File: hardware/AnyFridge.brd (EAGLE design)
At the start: 75.9 x 69.8 mm, 11 parts

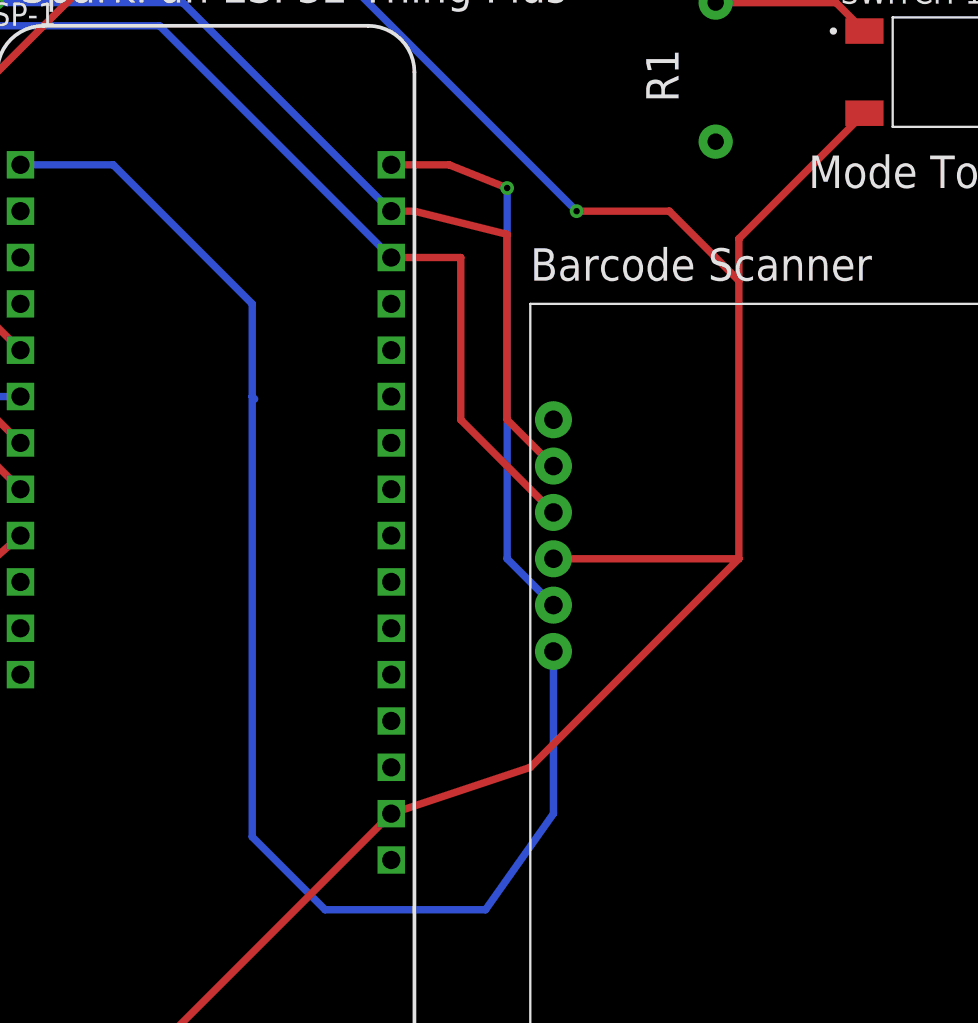
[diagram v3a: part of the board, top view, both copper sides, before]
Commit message: Align all traces to 45deg angles
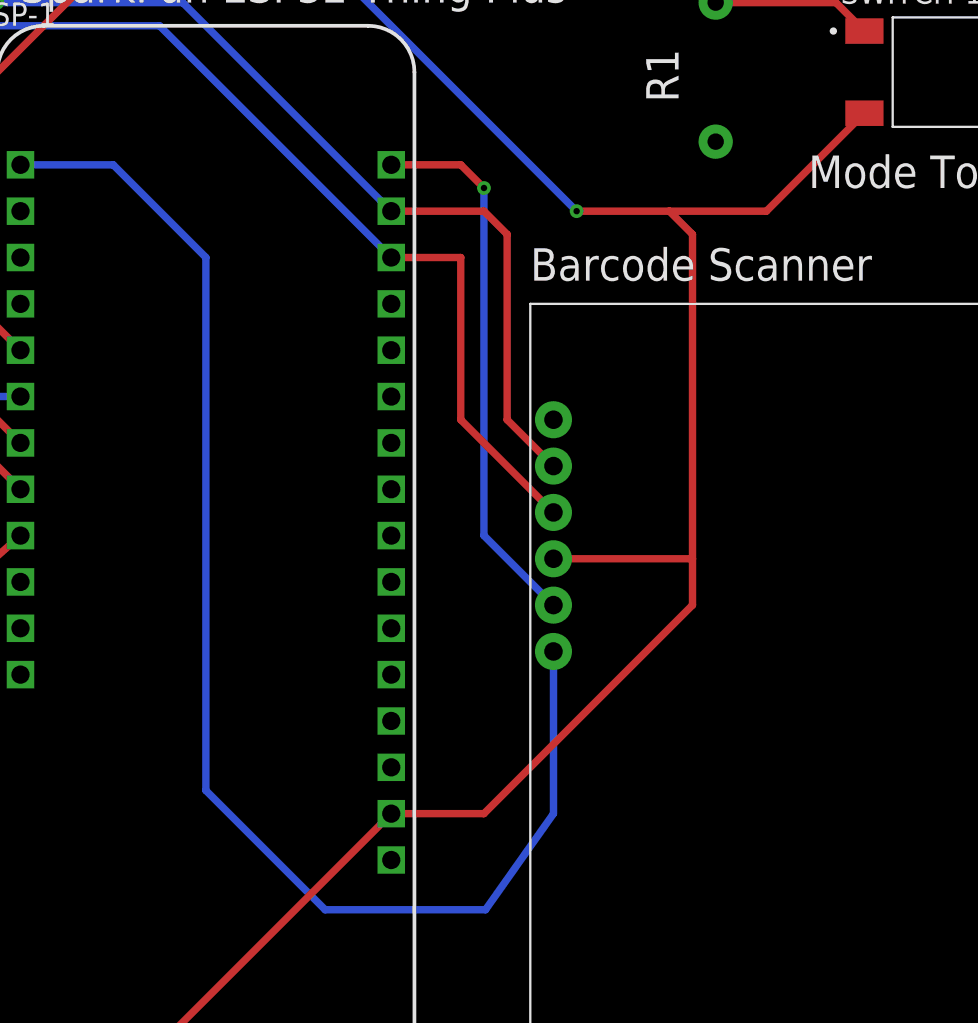
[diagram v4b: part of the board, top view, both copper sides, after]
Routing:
- net 3.3V: track 155.2 -> 152.1 mm
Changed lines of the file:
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@@
 <contactref element="SENS-1" pad="2"/>
 <contactref element="SWITCH-1" pad="2"/>
-<wire x1="66.57" y1="57.44" x2="59.69" y2="50.56" width="0.4064" layer="1"/>
-<wire x1="59.69" y1="50.56" x2="59.69" y2="48.26" width="0.4064" layer="1"/>
-<wire x1="59.69" y1="48.26" x2="59.69" y2="33.02" width="0.4064" layer="1"/>
-<wire x1="59.69" y1="33.02" x2="49.53" y2="33.02" width="0.4064" layer="1"/>
+<wire x1="57.15" y1="50.8" x2="57.15" y2="33.02" width="0.4064" layer="1"/>
+<wire x1="57.15" y1="33.02" x2="57.15" y2="30.48" width="0.4064" layer="1"/>
+<wire x1="57.15" y1="33.02" x2="49.53" y2="33.02" width="0.4064" layer="1"/>
 <contactref element="TP_3.3V" pad="TP"/>
 <wire x1="13.97" y1="66.04" x2="36.83" y2="66.04" width="0.4064" layer="16"/>
@@
 <via x="50.8" y="52.07" extent="1-16" drill="0.35"/>
 <wire x1="50.8" y1="52.07" x2="55.88" y2="52.07" width="0.4064" layer="1"/>
-<wire x1="55.88" y1="52.07" x2="59.69" y2="48.26" width="0.4064" layer="1"/>
+<wire x1="55.88" y1="52.07" x2="57.15" y2="50.8" width="0.4064" layer="1"/>
 <wire x1="40.64" y1="19.05" x2="24.13" y2="2.54" width="0.4064" layer="1"/>
 <wire x1="24.13" y1="2.54" x2="8.89" y2="2.54" width="0.4064" layer="1"/>
 <wire x1="8.89" y1="2.54" x2="8.255" y2="3.175" width="0.4064" layer="1"/>
 <wire x1="8.255" y1="3.175" x2="8.255" y2="4.18" width="0.4064" layer="1"/>
-<wire x1="40.64" y1="19.05" x2="48.26" y2="21.59" width="0.4064" layer="1"/>
-<wire x1="48.26" y1="21.59" x2="59.69" y2="33.02" width="0.4064" layer="1"/>
+<wire x1="57.15" y1="30.48" x2="45.72" y2="19.05" width="0.4064" layer="1"/>
+<wire x1="45.72" y1="19.05" x2="40.64" y2="19.05" width="0.4064" layer="1"/>
+<wire x1="66.57" y1="57.44" x2="61.2" y2="52.07" width="0.4064" layer="1"/>
+<wire x1="61.2" y1="52.07" x2="55.88" y2="52.07" width="0.4064" layer="1"/>
 </signal>
 <signal name="TRIG">
 <contactref element="SCAN-1" pad="TRIG"/>
 <contactref element="ESP-1" pad="21"/>
-<wire x1="46.99" y1="53.34" x2="43.815" y2="54.61" width="0.4064" layer="1"/>
-<wire x1="40.64" y1="54.61" x2="43.815" y2="54.61" width="0.4064" layer="1"/>
-<via x="46.99" y="53.34" extent="1-16" drill="0.35"/>
-<wire x1="46.99" y1="33.02" x2="49.53" y2="30.48" width="0.4064" layer="16"/>
-<wire x1="46.99" y1="33.02" x2="46.99" y2="53.34" width="0.4064" layer="16"/>
+<via x="45.72" y="53.34" extent="1-16" drill="0.35"/>
+<wire x1="45.72" y1="34.29" x2="49.53" y2="30.48" width="0.4064" layer="16"/>
+<wire x1="45.72" y1="53.34" x2="45.72" y2="34.29" width="0.4064" layer="16"/>
+<wire x1="45.72" y1="53.34" x2="44.45" y2="54.61" width="0.4064" layer="1"/>
+<wire x1="44.45" y1="54.61" x2="40.64" y2="54.61" width="0.4064" layer="1"/>
 </signal>
 <signal name="STAT">
 <contactref element="SCAN-1" pad="STAT"/>
 <contactref element="ESP-1" pad="23"/>
-<wire x1="33.02" y1="46.99" x2="25.4" y2="54.61" width="0.4064" layer="16"/>
+<wire x1="30.48" y1="49.53" x2="25.4" y2="54.61" width="0.4064" layer="16"/>
 <wire x1="20.32" y1="54.61" x2="25.4" y2="54.61" width="0.4064" layer="16"/>
-<wire x1="33.02" y1="41.91" x2="33.155425" y2="41.774575" width="0.4064" layer="16"/>
 <wire x1="49.53" y1="27.94" x2="49.53" y2="19.05" width="0.4064" layer="16"/>
 <wire x1="49.53" y1="19.05" x2="45.807071875" y2="13.784503125" width="0.4064" layer="16"/>
 <wire x1="45.807071875" y1="13.784503125" x2="37.015496875" y2="13.784503125" width="0.4064" layer="16"/>
-<wire x1="37.015496875" y1="13.784503125" x2="33.02" y2="17.78" width="0.4064" layer="16"/>
-<wire x1="33.02" y1="17.78" x2="33.02" y2="41.91" width="0.4064" layer="16"/>
-<wire x1="33.02" y1="41.91" x2="33.02" y2="46.99" width="0.4064" layer="16"/>
+<wire x1="37.015496875" y1="13.784503125" x2="30.48" y2="20.32" width="0.4064" layer="16"/>
+<wire x1="30.48" y1="20.32" x2="30.48" y2="49.53" width="0.4064" layer="16"/>
 </signal>
 <signal name="RED">
@@
 <contactref element="ESP-1" pad="17"/>
 <contactref element="SCAN-1" pad="RX"/>
-<wire x1="40.64" y1="52.07" x2="41.91" y2="52.07" width="0.4064" layer="1"/>
-<wire x1="46.99" y1="50.8" x2="41.91" y2="52.07" width="0.4064" layer="1"/>
-<wire x1="46.99" y1="50.8" x2="46.99" y2="40.64" width="0.4064" layer="1"/>
+<wire x1="46.99" y1="40.64" x2="46.99" y2="50.8" width="0.4064" layer="1"/>
 <wire x1="46.99" y1="40.64" x2="49.53" y2="38.1" width="0.4064" layer="1"/>
 <contactref element="TP_TX" pad="TP"/>
@@
 <wire x1="19.05" y1="63.5" x2="29.21" y2="63.5" width="0.4064" layer="16"/>
 <wire x1="29.21" y1="63.5" x2="40.64" y2="52.07" width="0.4064" layer="16"/>
+<wire x1="46.99" y1="50.8" x2="45.72" y2="52.07" width="0.4064" layer="1"/>
+<wire x1="45.72" y1="52.07" x2="40.64" y2="52.07" width="0.4064" layer="1"/>
 </signal>
 <signal name="RX1">
